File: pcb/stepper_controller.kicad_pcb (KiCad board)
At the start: 2 copper layers, 113 x 53.3 mm, 13 parts, among them P1 DBNC_INPUT, P2 DRIVE, P3 +24VDC, P4 INT_STEPPER, P5 INT_TONE, U1 MAX6817

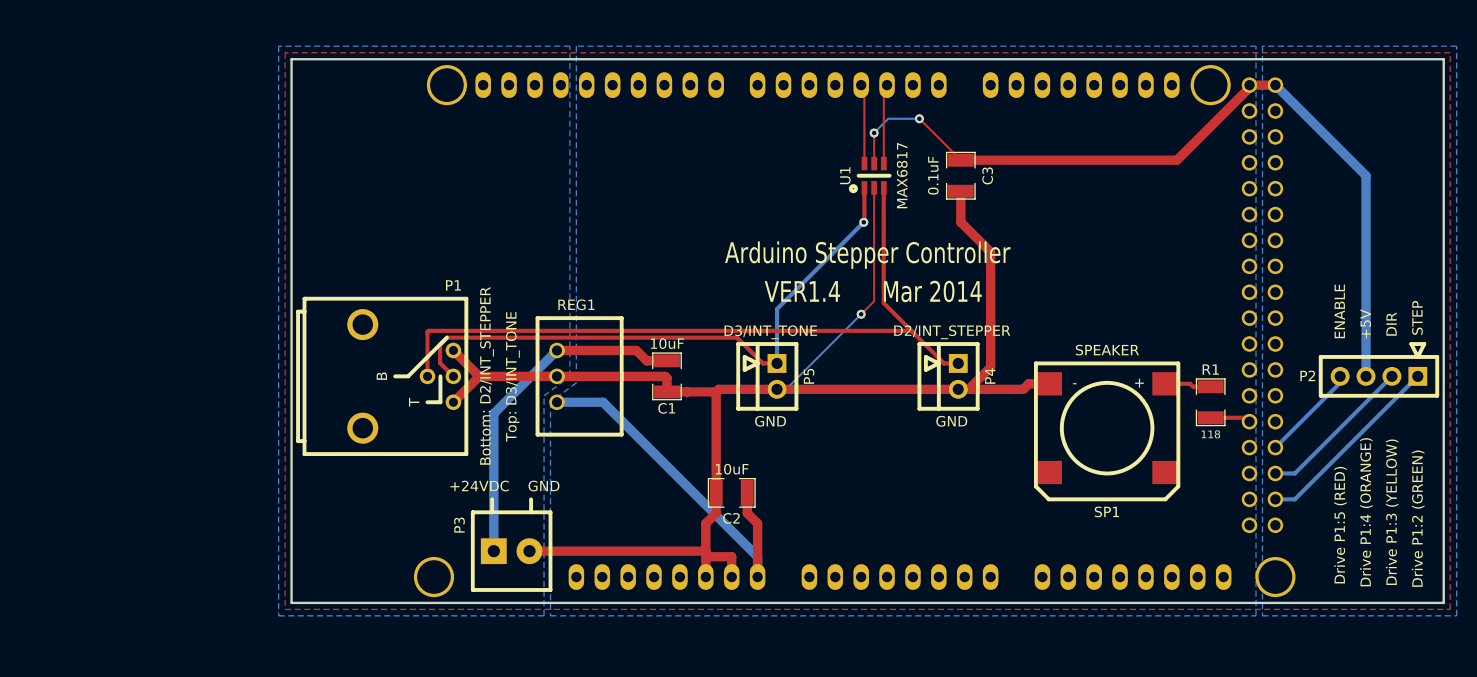
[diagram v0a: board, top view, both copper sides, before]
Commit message: Major changes to prepare for pcb mounted stepper driver.
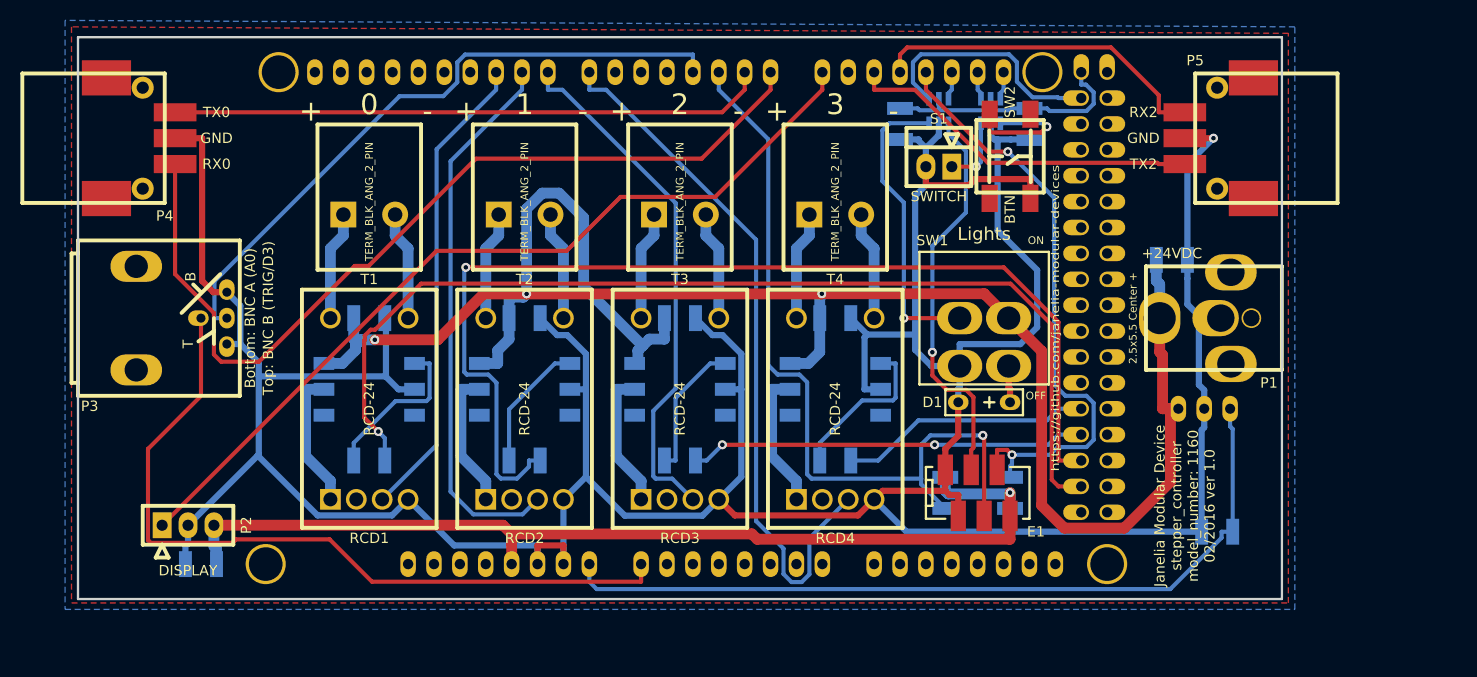
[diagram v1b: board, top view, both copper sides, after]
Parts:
- removed SHIELD1: ARDUINO_MEGA_SHIELD_FULL, ARDUINO_MEGA_SHIELD
- removed SP1: SPEAKER, SMS-1308MS-2-R
- added ARDUINO1: ARDUINO_MEGA, stepper_controller:ARDUINO_MEGA_SHIELD, F.Cu at (97.8, 129.5)
- added C4: 0.1uF, stepper_controller:SM1210, B.Cu at (174.0, 83.8)
- added C5: 0.1uF, stepper_controller:SM1210, B.Cu at (186.7, 83.8)
- added C6: 10uF, stepper_controller:SM1210, B.Cu at (121.9, 102.9)
- added C7: 10uF, stepper_controller:SM1210, B.Cu at (137.2, 102.9)
- added C8: 10uF, stepper_controller:SM1210, B.Cu at (152.4, 102.9)
- added C9: 10uF, stepper_controller:SM1210, B.Cu at (167.6, 102.9)
- added D1: LED_24V, stepper_controller:LED_555-3XXX, F.Cu at (182.2, 111.1)
- added E1: ENCODER_C14, stepper_controller:Micro-MaTch_6_SMD, F.Cu at (181.6, 120.0)
- added R2: 5.11k, stepper_controller:SM1210, B.Cu at (178.4, 120.0)
- added R3: 150, stepper_controller:SM1210, B.Cu at (121.9, 116.8)
- added R4: 150, stepper_controller:SM1210, B.Cu at (137.2, 116.8)
- added R5: 150, stepper_controller:SM1210, B.Cu at (152.4, 116.8)
- added R6: 150, stepper_controller:SM1210, B.Cu at (167.6, 116.8)
- added RCD1: RCD-24, stepper_controller:RCD-24, F.Cu at (121.9, 111.8)
- added RCD2: RCD-24, stepper_controller:RCD-24, F.Cu at (137.2, 111.8)
- added RCD3: RCD-24, stepper_controller:RCD-24, F.Cu at (152.4, 111.8)
- added RCD4: RCD-24, stepper_controller:RCD-24, F.Cu at (167.6, 111.8)
- added S1: HEADER_01X02_SHR, stepper_controller:Header_Shrouded_2_Pin, F.Cu at (177.8, 88.0)
- added SW1: DPST_SERIES_M, stepper_controller:DPST_SERIES_M, F.Cu at (182.2, 102.9)
- added SW2: KT_SWITCH, stepper_controller:KT_SWITCH, F.Cu at (184.8, 87.0)
- added T1: TERM_BLK_ANG_2_PIN, stepper_controller:TERM_BLK_ANG_2_PIN, F.Cu at (121.9, 92.7)
- added T2: TERM_BLK_ANG_2_PIN, stepper_controller:TERM_BLK_ANG_2_PIN, F.Cu at (137.2, 92.7)
- added T3: TERM_BLK_ANG_2_PIN, stepper_controller:TERM_BLK_ANG_2_PIN, F.Cu at (152.4, 92.7)
- added T4: TERM_BLK_ANG_2_PIN, stepper_controller:TERM_BLK_ANG_2_PIN, F.Cu at (167.6, 92.7)
- added U2: MAX6817, stepper_controller:MAX6817, B.Cu at (182.9, 82.5)
- added U3: SSR_DC_6PIN, stepper_controller:ASSR-1611, B.Cu at (121.9, 109.9)
- added U4: SSR_DC_6PIN, stepper_controller:ASSR-1611, B.Cu at (137.2, 109.9)
- added U5: SSR_DC_6PIN, stepper_controller:ASSR-1611, B.Cu at (152.4, 109.9)
- added U6: SSR_DC_6PIN, stepper_controller:ASSR-1611, B.Cu at (167.6, 109.9)
- C1, C2: footprint SM1210 -> stepper_controller:SM1210; moved to B.Cu
- C3: value 0.1uF -> 10uF; footprint SM1210 -> stepper_controller:SM1210; moved to B.Cu
- P1: value DBNC_INPUT -> PWR_JACK_2.5x5.5; footprint BNC_DOUBLE -> stepper_controller:DCJACK_2PIN_HIGHCURRENT
- P2: value DRIVE -> HEADER_01X03; footprint Header_4_Pin -> stepper_controller:Header_3_Pin
- P3: value +24VDC -> BNC_DOUBLE_RA; footprint TERMINAL_BLOCK_2POS_3.5mm -> stepper_controller:BNC_DOUBLE
- P4: value INT_STEPPER -> HEADER_01X03_SMD_RA; footprint Header_Shrouded_2_Pin -> stepper_controller:Header_3_Pin_SMD_RA
- P5: value INT_TONE -> HEADER_01X03_SMD_RA; footprint Header_Shrouded_2_Pin -> stepper_controller:Header_3_Pin_SMD_RA
- R1: value 118 -> 5.11k; footprint SM1210 -> stepper_controller:SM1210; moved to B.Cu
- REG1: value CONV_DC_DC -> CONV_DC_DC_12V_1A; footprint DC_DC_CONV_R78C -> stepper_controller:DC_DC_CONV_R78C; moved to B.Cu
- U1: footprint MAX6817 -> stepper_controller:MAX6817; moved to B.Cu
- moved P2 117.7 mm to (104.1, 123.2), turned to 180 degrees
- moved P1 90.4 mm to (211.5, 102.9), turned to 270 degrees
- moved P4 86.8 mm to (96.1, 85.2)
- moved C3 83.7 mm to (105.4, 127.0), turned to 180 degrees
- moved REG1 63.6 mm to (203.8, 111.8), turned to 0 degrees
- moved P5 52.3 mm to (208.7, 85.2), turned to 270 degrees
- moved C1 50.8 mm to (200.7, 97.2), turned to 0 degrees
- moved C2 47.8 mm to (205.1, 123.8)
- moved P3 43.3 mm to (99.1, 102.9), turned to 90 degrees
- moved R1 21.6 mm to (184.8, 120.0), turned to 90 degrees
- moved U1 8.98 mm to (177.8, 82.5)
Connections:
- net /VIN renamed /V_IN
- P1 pad 1: /INT_STEPPER -> VAA
- P2 pad 1: /STEP -> /TX3
- P2 pad 2: /DIR -> GND
- P3 pad 1: VAA -> /BNC_A
- P4 pad 1: /INT_STEPPER -> /RX0
- P5 pad 1: /INT_TONE -> /RX2
- R1 pad 1: N-000087 -> +5V
- R1 pad 2: /SPEAKER -> /ENC_A
- U1 pad 1: /INT_TONE -> /ENC_BTN
- U1 pad 3: /INT_STEPPER -> /LIGHTS
- U1 pad 4: /INT_STEPPER_DEBOUNCED -> /D_LIGHTS
- U1 pad 5: +5V -> +5VD
- U1 pad 6: /INT_TONE_DEBOUNCED -> /D_ENC_BTN
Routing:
- net GND: track 152.0 -> 395.1 mm
- net VAA: track 33.5 -> 189.7 mm, vias 0 -> 3
- net /ENABLE_1: track 0.00 -> 104.6 mm, vias 0 -> 1
- net /ENABLE_0: track 0.00 -> 102.7 mm, vias 0 -> 1
- net /RX0: track 0.00 -> 87.9 mm
- net /TX3: track 0.00 -> 84.2 mm
- net /ENC_B: track 0.00 -> 77.3 mm, vias 0 -> 1
- net /BNC_A: track 0.00 -> 76.0 mm
- net /INT_STEPPER: track 72.9 -> 0.00 mm
- net /PWM_3: track 0.00 -> 70.2 mm
- net /BNC_B: track 0.00 -> 63.9 mm
- net /ENC_A: track 0.00 -> 59.8 mm, vias 0 -> 2
- net /INT_TONE: track 58.8 -> 0.00 mm, vias 1 -> 0
- net /TX0: track 0.00 -> 58.5 mm
- net /PWM_1: track 0.00 -> 54.1 mm
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- added copper zone on B.Cu, net GND
- added copper zone on F.Cu, net VAA
- removed copper zone on B.Cu, net +5V
- removed copper zone on B.Cu, net /V_IN
- removed copper zone on F.Cu, net GND
- removed copper zone on B.Cu, net VAA
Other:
- board size 113 x 53.3 mm -> 118.1 x 55.1 mm
- net class Default: trace_width 0.2032 -> 0.254
- net class GND added: clearance 0.254, trace_width 0.6096, via_dia 0.889, via_drill 0.635
- net class LED_POWER added: clearance 0.254, trace_width 0.6096, via_dia 0.889, via_drill 0.635
- net class POWER: trace_width 0.9144 -> 1.0668
- rule pad_to_mask_clearance: 0.254 -> 0
- rule trace_min: 0.2032 -> 0.254
- board text added: "+"
- board text added: "+24VDC"
- board text added: "-"
- board text added: "0"
- board text added: "1"
- board text added: "12V_DC_DC"
- board text added: "2"
- board text added: "2.5x5.5 Center +"
- board text added: "3"
- board text added: "DISPLAY"
- board text added: "Janelia Modular Device stepper_controller model_number: 1160 02/2016 ver 1.0"
- board text added: "SWITCH"
- board text added: "https://github.com/janelia-modular-devices"
- board text removed: "+5V"
- board text removed: "Arduino Stepper Controller"
- board text removed: "Bottom: D2/INT_STEPPER"
- board text removed: "D2/INT_STEPPER"
- board text removed: "D3/INT_TONE"
- board text removed: "DIR"
- board text removed: "Drive P1:2 (GREEN)"
- board text removed: "Drive P1:3 (YELLOW)"
- board text removed: "Drive P1:4 (ORANGE)"
- board text removed: "Drive P1:5 (RED)"
- board text removed: "ENABLE"
- board text removed: "GND"
- board text removed: "Mar 2014"
- board text removed: "STEP"
- board text removed: "Top: D3/INT_TONE"
- board text removed: "VER1.4"

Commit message: Use power_switch_controller as base for pcb.
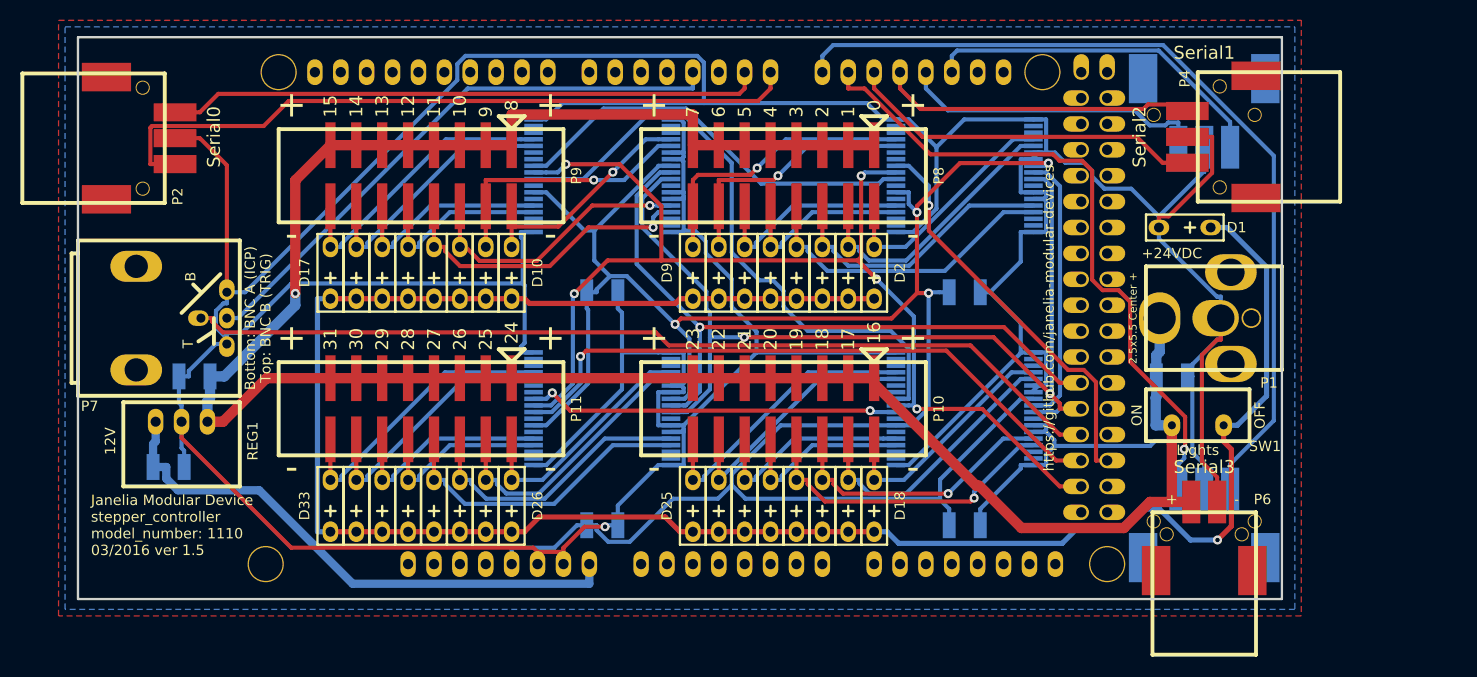
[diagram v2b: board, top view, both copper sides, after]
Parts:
- removed C8, C9: 10uF, stepper_controller:SM1210
- removed E1: ENCODER_C14, stepper_controller:Micro-MaTch_6_SMD
- removed R1, R2: 5.11k, stepper_controller:SM1210
- removed R3, R4, R5, R6: 150, stepper_controller:SM1210
- removed RCD1, RCD2, RCD3, RCD4: RCD-24, stepper_controller:RCD-24
- removed S1: HEADER_01X02_SHR, stepper_controller:Header_Shrouded_2_Pin
- removed SW2: KT_SWITCH, stepper_controller:KT_SWITCH
- removed T1, T2, T3, T4: TERM_BLK_ANG_2_PIN, stepper_controller:TERM_BLK_ANG_2_PIN
- removed U5, U6: SSR_DC_6PIN, stepper_controller:ASSR-1611
- added D10: LED_24V, stepper_controller:LED_555-3XXX, F.Cu at (135.9, 98.4)
- added D11: LED_24V, stepper_controller:LED_555-3XXX, F.Cu at (133.3, 98.4)
- added D12: LED_24V, stepper_controller:LED_555-3XXX, F.Cu at (130.8, 98.4)
- added D13: LED_24V, stepper_controller:LED_555-3XXX, F.Cu at (128.3, 98.4)
- added D14: LED_24V, stepper_controller:LED_555-3XXX, F.Cu at (125.7, 98.4)
- added D15: LED_24V, stepper_controller:LED_555-3XXX, F.Cu at (123.2, 98.4)
- added D16: LED_24V, stepper_controller:LED_555-3XXX, F.Cu at (120.7, 98.4)
- added D17: LED_24V, stepper_controller:LED_555-3XXX, F.Cu at (118.1, 98.4)
- added D18: LED_24V, stepper_controller:LED_555-3XXX, F.Cu at (171.4, 121.3)
- added D19: LED_24V, stepper_controller:LED_555-3XXX, F.Cu at (168.9, 121.3)
- added D2: LED_24V, stepper_controller:LED_555-3XXX, F.Cu at (171.4, 98.4)
- added D20: LED_24V, stepper_controller:LED_555-3XXX, F.Cu at (166.4, 121.3)
- added D21: LED_24V, stepper_controller:LED_555-3XXX, F.Cu at (163.8, 121.3)
- added D22: LED_24V, stepper_controller:LED_555-3XXX, F.Cu at (161.3, 121.3)
- added D23: LED_24V, stepper_controller:LED_555-3XXX, F.Cu at (158.8, 121.3)
- added D24: LED_24V, stepper_controller:LED_555-3XXX, F.Cu at (156.2, 121.3)
- added D25: LED_24V, stepper_controller:LED_555-3XXX, F.Cu at (153.7, 121.3)
- added D26: LED_24V, stepper_controller:LED_555-3XXX, F.Cu at (135.9, 121.3)
- added D27: LED_24V, stepper_controller:LED_555-3XXX, F.Cu at (133.3, 121.3)
- added D28: LED_24V, stepper_controller:LED_555-3XXX, F.Cu at (130.8, 121.3)
- added D29: LED_24V, stepper_controller:LED_555-3XXX, F.Cu at (128.3, 121.3)
- added D3: LED_24V, stepper_controller:LED_555-3XXX, F.Cu at (168.9, 98.4)
- added D30: LED_24V, stepper_controller:LED_555-3XXX, F.Cu at (125.7, 121.3)
- added D31: LED_24V, stepper_controller:LED_555-3XXX, F.Cu at (123.2, 121.3)
- added D32: LED_24V, stepper_controller:LED_555-3XXX, F.Cu at (120.7, 121.3)
- added D33: LED_24V, stepper_controller:LED_555-3XXX, F.Cu at (118.1, 121.3)
- added D4: LED_24V, stepper_controller:LED_555-3XXX, F.Cu at (166.4, 98.4)
- added D5: LED_24V, stepper_controller:LED_555-3XXX, F.Cu at (163.8, 98.4)
- added D6: LED_24V, stepper_controller:LED_555-3XXX, F.Cu at (161.3, 98.4)
- added D7: LED_24V, stepper_controller:LED_555-3XXX, F.Cu at (158.8, 98.4)
- added D8: LED_24V, stepper_controller:LED_555-3XXX, F.Cu at (156.2, 98.4)
- added D9: LED_24V, stepper_controller:LED_555-3XXX, F.Cu at (153.7, 98.4)
- added P10: HEADER_02X08_SMD, stepper_controller:HEADER_02x08_SMD, F.Cu at (162.6, 111.8)
- added P11: HEADER_02X08_SMD, stepper_controller:HEADER_02x08_SMD, F.Cu at (127.0, 111.8)
- added P6: HEADER_01X02_SMD_RA, stepper_controller:Header_2_Pin_SMD_RA, F.Cu at (203.8, 127.6)
- added P7: BNC_DOUBLE_RA, stepper_controller:BNC_DOUBLE, F.Cu at (99.1, 102.9)
- added P8: HEADER_02X08_SMD, stepper_controller:HEADER_02x08_SMD, F.Cu at (162.6, 88.9)
- added P9: HEADER_02X08_SMD, stepper_controller:HEADER_02x08_SMD, F.Cu at (127.0, 88.9)
- C6, C7: value 10uF -> 0.1uF
- P2: value HEADER_01X03 -> HEADER_01X03_SMD_RA; footprint stepper_controller:Header_3_Pin -> stepper_controller:Header_3_Pin_SMD_RA
- P3: value BNC_DOUBLE_RA -> HEADER_01X03_SMD_RA; footprint stepper_controller:BNC_DOUBLE -> stepper_controller:Header_3_Pin_SMD_RA; moved to B.Cu
- P5: moved to B.Cu
- REG1: moved to F.Cu
- SW1: value DPST_SERIES_M -> SPST_SLIDE_AS; footprint stepper_controller:DPST_SERIES_M -> stepper_controller:SPST_SLIDE_AS
- U1, U2: value MAX6817 -> TLE7230R; footprint stepper_controller:MAX6817 -> stepper_controller:PG-DSO-36
- U3, U4: value SSR_DC_6PIN -> TLE7230R; footprint stepper_controller:ASSR-1611 -> stepper_controller:PG-DSO-36
- moved P4 112.8 mm to (208.9, 85.1), turned to 270 degrees
- moved P3 107.4 mm to (203.8, 79.4), turned to 180 degrees
- moved C2 101.5 mm to (104.8, 108.6)
- moved REG1 100.3 mm to (103.5, 113.0), turned to 180 degrees
- moved C6 61.9 mm to (180.3, 123.2)
- moved U3 58.5 mm to (180.3, 111.8), turned to 270 degrees
- moved C5 45.0 mm to (144.8, 100.3), turned to 0 degrees
- moved P5 41.4 mm to (203.8, 126.4), turned to 0 degrees
- moved P2 38.8 mm to (96.1, 85.2), turned to 90 degrees
- moved U2 38.6 mm to (144.8, 88.9), turned to 270 degrees
- moved D1 26.1 mm to (201.9, 94.0)
- moved SW1 23.0 mm to (203.2, 112.4), turned to 90 degrees
- moved C7 21.7 mm to (144.8, 123.2)
- moved C4 17.7 mm to (180.3, 100.3), turned to 0 degrees
- moved C1 11.4 mm to (200.7, 108.6)
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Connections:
- ARDUINO1 pad 10: /PWM_0 -> (no net)
- ARDUINO1 pad 11: Net-(ARDUINO1-Pad11) -> (no net)
- ARDUINO1 pad 12: Net-(ARDUINO1-Pad12) -> (no net)
- ARDUINO1 pad 13: Net-(ARDUINO1-Pad13) -> (no net)
- ARDUINO1 pad 15: Net-(ARDUINO1-Pad15) -> /RX3
- ARDUINO1 pad 18: /ENC_A -> /TX1
- ARDUINO1 pad 19: /D_ENC_BTN -> /RX1
- ARDUINO1 pad 2: /ENC_B -> (no net)
- ARDUINO1 pad 20: /D_SWITCH -> (no net)
- ARDUINO1 pad 20B: Net-(ARDUINO1-Pad20B) -> (no net)
- ARDUINO1 pad 21: /D_BTN -> (no net)
- ARDUINO1 pad 21B: Net-(ARDUINO1-Pad21B) -> (no net)
- ARDUINO1 pad 22: /D_LIGHTS -> (no net)
- ARDUINO1 pad 23: Net-(ARDUINO1-Pad23) -> (no net)
- ARDUINO1 pad 24: Net-(ARDUINO1-Pad24) -> (no net)
- ARDUINO1 pad 25: Net-(ARDUINO1-Pad25) -> (no net)
- ARDUINO1 pad 26: Net-(ARDUINO1-Pad26) -> (no net)
- ARDUINO1 pad 27: Net-(ARDUINO1-Pad27) -> (no net)
- ARDUINO1 pad 28: Net-(ARDUINO1-Pad28) -> (no net)
- ARDUINO1 pad 29: Net-(ARDUINO1-Pad29) -> (no net)
- ARDUINO1 pad 30: Net-(ARDUINO1-Pad30) -> (no net)
- ARDUINO1 pad 31: Net-(ARDUINO1-Pad31) -> (no net)
- ARDUINO1 pad 32: Net-(ARDUINO1-Pad32) -> (no net)
- ARDUINO1 pad 33: Net-(ARDUINO1-Pad33) -> (no net)
- ARDUINO1 pad 34: Net-(ARDUINO1-Pad34) -> (no net)
- ARDUINO1 pad 35: Net-(ARDUINO1-Pad35) -> (no net)
- ARDUINO1 pad 36: Net-(ARDUINO1-Pad36) -> (no net)
- ARDUINO1 pad 37: Net-(ARDUINO1-Pad37) -> (no net)
- ARDUINO1 pad 38: Net-(ARDUINO1-Pad38) -> (no net)
- ARDUINO1 pad 39: Net-(ARDUINO1-Pad39) -> (no net)
- ARDUINO1 pad 3V3: Net-(ARDUINO1-Pad3V3) -> (no net)
- ARDUINO1 pad 4: Net-(ARDUINO1-Pad4) -> (no net)
- ARDUINO1 pad 40: Net-(ARDUINO1-Pad40) -> (no net)
- ARDUINO1 pad 41: Net-(ARDUINO1-Pad41) -> (no net)
- ARDUINO1 pad 42: Net-(ARDUINO1-Pad42) -> (no net)
- ARDUINO1 pad 43: Net-(ARDUINO1-Pad43) -> (no net)
- ARDUINO1 pad 44: Net-(ARDUINO1-Pad44) -> /RESET
- ARDUINO1 pad 45: Net-(ARDUINO1-Pad45) -> (no net)
- ARDUINO1 pad 46: /ENABLE_3 -> /CS
- ARDUINO1 pad 47: Net-(ARDUINO1-Pad47) -> (no net)
- ARDUINO1 pad 48: /ENABLE_2 -> /BNC_A
- ARDUINO1 pad 49: Net-(ARDUINO1-Pad49) -> (no net)
- ARDUINO1 pad 5: Net-(ARDUINO1-Pad5) -> (no net)
- ARDUINO1 pad 50: /ENABLE_1 -> /MISO
- ARDUINO1 pad 51: Net-(ARDUINO1-Pad51) -> /MOSI
- ARDUINO1 pad 52: /ENABLE_0 -> /SCK
- ARDUINO1 pad 53: Net-(ARDUINO1-Pad53) -> (no net)
- ARDUINO1 pad 5V_4: +5VD -> (no net)
- ARDUINO1 pad 5V_5: Net-(ARDUINO1-Pad5V_5) -> (no net)
- ARDUINO1 pad 6: Net-(ARDUINO1-Pad6) -> (no net)
- ARDUINO1 pad 7: /PWM_3 -> (no net)
- ARDUINO1 pad 8: /PWM_2 -> (no net)
- ARDUINO1 pad 9: /PWM_1 -> (no net)
- ARDUINO1 pad A0: /BNC_A -> (no net)
- ARDUINO1 pad A1: Net-(ARDUINO1-PadA1) -> (no net)
- ARDUINO1 pad A10: Net-(ARDUINO1-PadA10) -> (no net)
- ARDUINO1 pad A11: Net-(ARDUINO1-PadA11) -> (no net)
- ARDUINO1 pad A12: Net-(ARDUINO1-PadA12) -> (no net)
- ARDUINO1 pad A13: Net-(ARDUINO1-PadA13) -> (no net)
- ARDUINO1 pad A14: Net-(ARDUINO1-PadA14) -> (no net)
- ARDUINO1 pad A15: Net-(ARDUINO1-PadA15) -> (no net)
- ARDUINO1 pad A2: Net-(ARDUINO1-PadA2) -> (no net)
- ARDUINO1 pad A3: Net-(ARDUINO1-PadA3) -> (no net)
- ARDUINO1 pad A4: Net-(ARDUINO1-PadA4) -> (no net)
- ARDUINO1 pad A5: Net-(ARDUINO1-PadA5) -> (no net)
- ARDUINO1 pad A6: Net-(ARDUINO1-PadA6) -> (no net)
- ARDUINO1 pad A7: Net-(ARDUINO1-PadA7) -> (no net)
- ARDUINO1 pad A8: Net-(ARDUINO1-PadA8) -> (no net)
- ARDUINO1 pad A9: Net-(ARDUINO1-PadA9) -> (no net)
- ARDUINO1 pad AREF: Net-(ARDUINO1-PadAREF) -> (no net)
- ARDUINO1 pad GND3: Net-(ARDUINO1-PadGND3) -> (no net)
- ARDUINO1 pad GND4: Net-(ARDUINO1-PadGND4) -> (no net)
- ARDUINO1 pad GND5: Net-(ARDUINO1-PadGND5) -> (no net)
- ARDUINO1 pad IREF: Net-(ARDUINO1-PadIREF) -> (no net)
- ARDUINO1 pad NC: Net-(ARDUINO1-PadNC) -> (no net)
- ARDUINO1 pad RST: Net-(ARDUINO1-PadRST) -> (no net)
- C2 pad 1: /V_IN -> VAA
- C3 pad 1: +5V -> /V_IN
- C4 pad 1: +5VD -> +5V
- C5 pad 1: +5VD -> +5V
- C6 pad 1: VAA -> +5V
- C7 pad 1: VAA -> +5V
- P2 pad 1: /TX3 -> /RX0
- P2 pad 3: +5V -> /TX0
- P3 pad 1: /BNC_A -> /RX1
- P3 pad 3: /BNC_B -> /TX1
- P4 pad 1: /RX0 -> /RX2
- P4 pad 3: /TX0 -> /TX2
- P5 pad 1: /RX2 -> /RX3
- P5 pad 3: /TX2 -> /TX3
- U1 pad 1: /ENC_BTN -> GND
- U1 pad 2: GND -> (no net)
- U1 pad 3: /LIGHTS -> (no net)
- U1 pad 4: /D_LIGHTS -> /OUT0
- U1 pad 5: +5VD -> /OUT1
- U1 pad 6: /D_ENC_BTN -> GND
- U2 pad 1: /BTN -> GND
- U2 pad 2: GND -> (no net)
- U2 pad 3: /SWITCH -> (no net)
- U2 pad 4: /D_SWITCH -> /OUT8
- U2 pad 5: +5VD -> /OUT9
- U2 pad 6: /D_BTN -> GND
- U3 pad 1: Net-(R3-Pad1) -> GND
- U3 pad 2: GND -> (no net)
- U3 pad 3: Net-(U3-Pad3) -> (no net)
- U3 pad 4: Net-(U3-Pad4) -> /OUT16
- U3 pad 5: /IN_0+ -> /OUT17
- U3 pad 6: VAA -> GND
- U4 pad 1: Net-(R4-Pad1) -> GND
- U4 pad 2: GND -> (no net)
- U4 pad 3: Net-(U4-Pad3) -> (no net)
- U4 pad 4: Net-(U4-Pad4) -> /OUT24
- U4 pad 5: /IN_1+ -> /OUT25
- U4 pad 6: VAA -> GND
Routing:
- net /LED_PWR: track 3.64 -> 207.8 mm, vias 0 -> 1
- net GND: track 395.1 -> 558.3 mm
- net +5V: track 99.5 -> 216.2 mm, vias 1 -> 4
- net /SCK: track 0.00 -> 112.7 mm, vias 0 -> 5
- net /ENABLE_1: track 104.6 -> 0.00 mm, vias 1 -> 0
- net /ENABLE_0: track 102.7 -> 0.00 mm, vias 1 -> 0
- net /RESET: track 0.00 -> 97.9 mm, vias 0 -> 1
- net /CS: track 0.00 -> 96.8 mm, vias 0 -> 2
- net /ENC_B: track 77.3 -> 0.00 mm, vias 1 -> 0
- net /PWM_3: track 70.2 -> 0.00 mm
- net /RX3: track 0.00 -> 65.1 mm, vias 0 -> 1
- net /MISO: track 0.00 -> 62.2 mm, vias 0 -> 1
- net /SO2: track 0.00 -> 61.2 mm
- net /ENC_A: track 59.8 -> 0.00 mm, vias 2 -> 0
- net /PWM_1: track 54.1 -> 0.00 mm
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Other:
- net class Default: clearance 0.254 -> 0.0254
- net class GND: clearance 0.254 -> 0.1016; trace_width 0.6096 -> 0.4064
- net class LEDPOWER added: clearance 0.254, trace_width 0.508, via_dia 0.889, via_drill 0.635
- net class LED_POWER removed
- net class POWER: trace_width 1.0668 -> 0.8128
- net class SIGNAL: clearance 0.254 -> 0.1016
- net class SUPERPOWER added: clearance 0.254, trace_width 1.016, via_dia 0.889, via_drill 0.635
- rule trace_clearance: 0.254 -> 0.0254
- board text added: "10"
- board text added: "11"
- board text added: "12"
- board text added: "12V"
- board text added: "13"
- board text added: "14"
- board text added: "15"
- board text added: "16"
- board text added: "17"
- board text added: "18"
- board text added: "19"
- board text added: "20"
- board text added: "21"
- board text added: "22"
- board text added: "23"
- board text added: "24"
- board text added: "25"
- board text added: "26"
- board text added: "27"
- board text added: "28"
- board text added: "29"
- board text added: "30"
- board text added: "31"
- board text added: "4"
- board text added: "5"
- board text added: "6"
- board text added: "7"
- board text added: "8"
- board text added: "9"
- board text added: "Janelia Modular Device stepper_controller model_number: 1110 03/2016 ver 1.5"
- board text added: "Lights"
- board text added: "Serial0"
- board text added: "Serial1"
- board text added: "Serial2"
- board text added: "Serial3"
- board text removed: "12V_DC_DC"
- board text removed: "DISPLAY"
- board text removed: "Janelia Modular Device stepper_controller model_number: 1160 02/2016 ver 1.0"
- board text removed: "SWITCH"

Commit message: Progress towards pcb 1.0.
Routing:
- net GND: track 558.3 -> 0.00 mm, vias 1 -> 0
- net VAA: track 217.8 -> 0.00 mm, vias 1 -> 0
- net +5V: track 216.2 -> 0.00 mm, vias 4 -> 0
- net /LED_PWR: track 207.8 -> 0.00 mm, vias 1 -> 0
- net /SCK: track 112.7 -> 0.00 mm, vias 5 -> 0
- net /RESET: track 97.9 -> 0.00 mm, vias 1 -> 0
- net /CS: track 96.8 -> 0.00 mm, vias 2 -> 0
- net /BNC_A: track 91.3 -> 0.00 mm
- net /TX3: track 85.3 -> 0.00 mm
- net /RX0: track 70.0 -> 0.00 mm
- net /RX3: track 65.1 -> 0.00 mm, vias 1 -> 0
- net /MISO: track 62.2 -> 0.00 mm, vias 1 -> 0
- net /SO2: track 61.2 -> 0.00 mm
- net /TX0: track 58.4 -> 0.00 mm
- net /BNC_B: track 56.7 -> 0.00 mm
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- removed copper zone on B.Cu, net GND
- removed copper zone on F.Cu, net VAA
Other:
- board text added: "Janelia Modular Device stepper_controller model_number: 1140 03/2016 ver 1.0"
- board text removed: "Janelia Modular Device stepper_controller model_number: 1110 03/2016 ver 1.5"
